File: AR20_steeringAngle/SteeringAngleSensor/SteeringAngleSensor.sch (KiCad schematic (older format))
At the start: 4 parts, among them J1 Conn_01x03_Female

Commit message: Added: 90deg JST XH connector
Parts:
- removed J1: Conn_01x03_Female, Connector_JST:JST_EH_B3B-EH-A_1x03_P2.50mm_Vertical, symbol Connector:Conn_01x03_Female
- added J1: Conn_01x04_Male, Connector_JST:JST_XH_S4B-XH-A_1x04_P2.50mm_Horizontal, symbol Connector:Conn_01x04_Male
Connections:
- net 5V: now also J1.3 (Pin_3)
- net GND: now also J1.1 (Pin_1)
- net Out: now also J1.2 (Pin_2)
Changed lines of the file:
@@
 EESchema Schematic File Version 4
+LIBS:SteeringAngleSensor-cache
 EELAYER 29 0
 EELAYER END
@@
 Comment4 ""
 $EndDescr
-$Comp
-L Connector:Conn_01x03_Female J1
-U 1 1 5E14CE43
-P 6125 3125
-F 0 "J1" H 6153 3151 50  0000 L CNN
-F 1 "Conn_01x03_Female" H 6153 3060 50  0000 L CNN
-F 2 "Connector_JST:JST_EH_B3B-EH-A_1x03_P2.50mm_Vertical" H 6125 3125 50  0001 C CNN
-F 3 "~" H 6125 3125 50  0001 C CNN
-	1    6125 3125
-	1    0    0    -1
-$EndComp
 Wire Wire Line
 	5575 2975 5750 2975
@@
 Text HLabel 5825 3300 2    50   Input ~ 0
 GND
+$Comp
+L Connector:Conn_01x04_Male J1
+U 1 1 5E14D28B
+P 6125 3125
+F 0 "J1" H 6097 3007 50  0000 R CNN
+F 1 "Conn_01x04_Male" H 6097 3098 50  0000 R CNN
+F 2 "Connector_JST:JST_XH_S4B-XH-A_1x04_P2.50mm_Horizontal" H 6125 3125 50  0001 C CNN
+F 3 "~" H 6125 3125 50  0001 C CNN
+	1    6125 3125
+	-1   0    0    1
+$EndComp
 $EndSCHEMATC

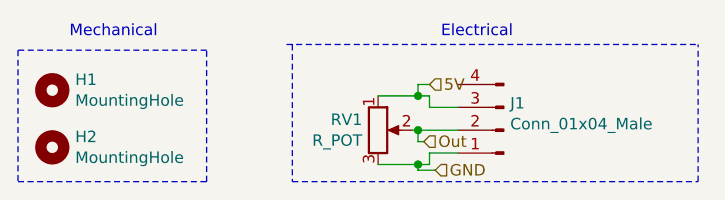
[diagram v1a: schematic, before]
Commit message: Connector change
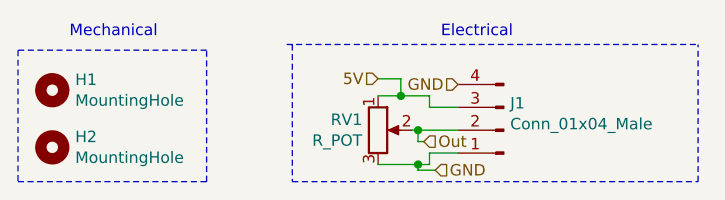
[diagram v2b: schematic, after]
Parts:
- J1: footprint Connector_JST:JST_XH_S4B-XH-A_1x04_P2.50mm_Horizontal -> Connector_JST:JST_PH_B4B-PH-SM4-TB_1x04-1MP_P2.00mm_Vertical
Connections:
- net GND: now also J1.4 (Pin_4)
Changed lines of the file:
@@
 $EndDescr
-Wire Wire Line
-	5575 2975 5750 2975
 Wire Wire Line
 	5925 3025 5800 3025
@@
 	5750 3125 5725 3125
 Wire Wire Line
-	5750 2975 5750 2925
-Wire Wire Line
-	5750 2925 5800 2925
-Connection ~ 5750 2975
-Wire Wire Line
-	5750 2975 5800 2975
-Wire Wire Line
 	5750 3275 5750 3300
 Wire Wire Line
@@
 Wire Wire Line
 	5750 3275 5575 3275
-Text HLabel 5800 2925 2    50   Input ~ 0
-5V
 Text HLabel 5775 3175 2    50   Input ~ 0
 Out
@@
 F 0 "J1" H 6097 3007 50  0000 R CNN
 F 1 "Conn_01x04_Male" H 6097 3098 50  0000 R CNN
-F 2 "Connector_JST:JST_XH_S4B-XH-A_1x04_P2.50mm_Horizontal" H 6125 3125 50  0001 C CNN
+F 2 "Connector_JST:JST_PH_B4B-PH-SM4-TB_1x04-1MP_P2.00mm_Vertical" H 6125 3125 50  0001 C CNN
 F 3 "~" H 6125 3125 50  0001 C CNN
 	1    6125 3125
 	-1   0    0    1
 $EndComp
+Text HLabel 5925 2925 0    50   Input ~ 0
+GND
+Wire Wire Line
+	5575 2975 5675 2975
+Text HLabel 5575 2900 0    50   Input ~ 0
+5V
+Wire Wire Line
+	5575 2900 5675 2900
+Wire Wire Line
+	5675 2900 5675 2975
+Connection ~ 5675 2975
+Wire Wire Line
+	5675 2975 5800 2975
 $EndSCHEMATC
